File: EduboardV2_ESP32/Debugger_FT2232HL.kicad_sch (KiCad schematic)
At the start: 52 parts, among them Q1 S8050_C139514, Q2 S8050_C139514, U2 FT2232HL, U3 M93C46-WMN6TP, Y2 12MHz

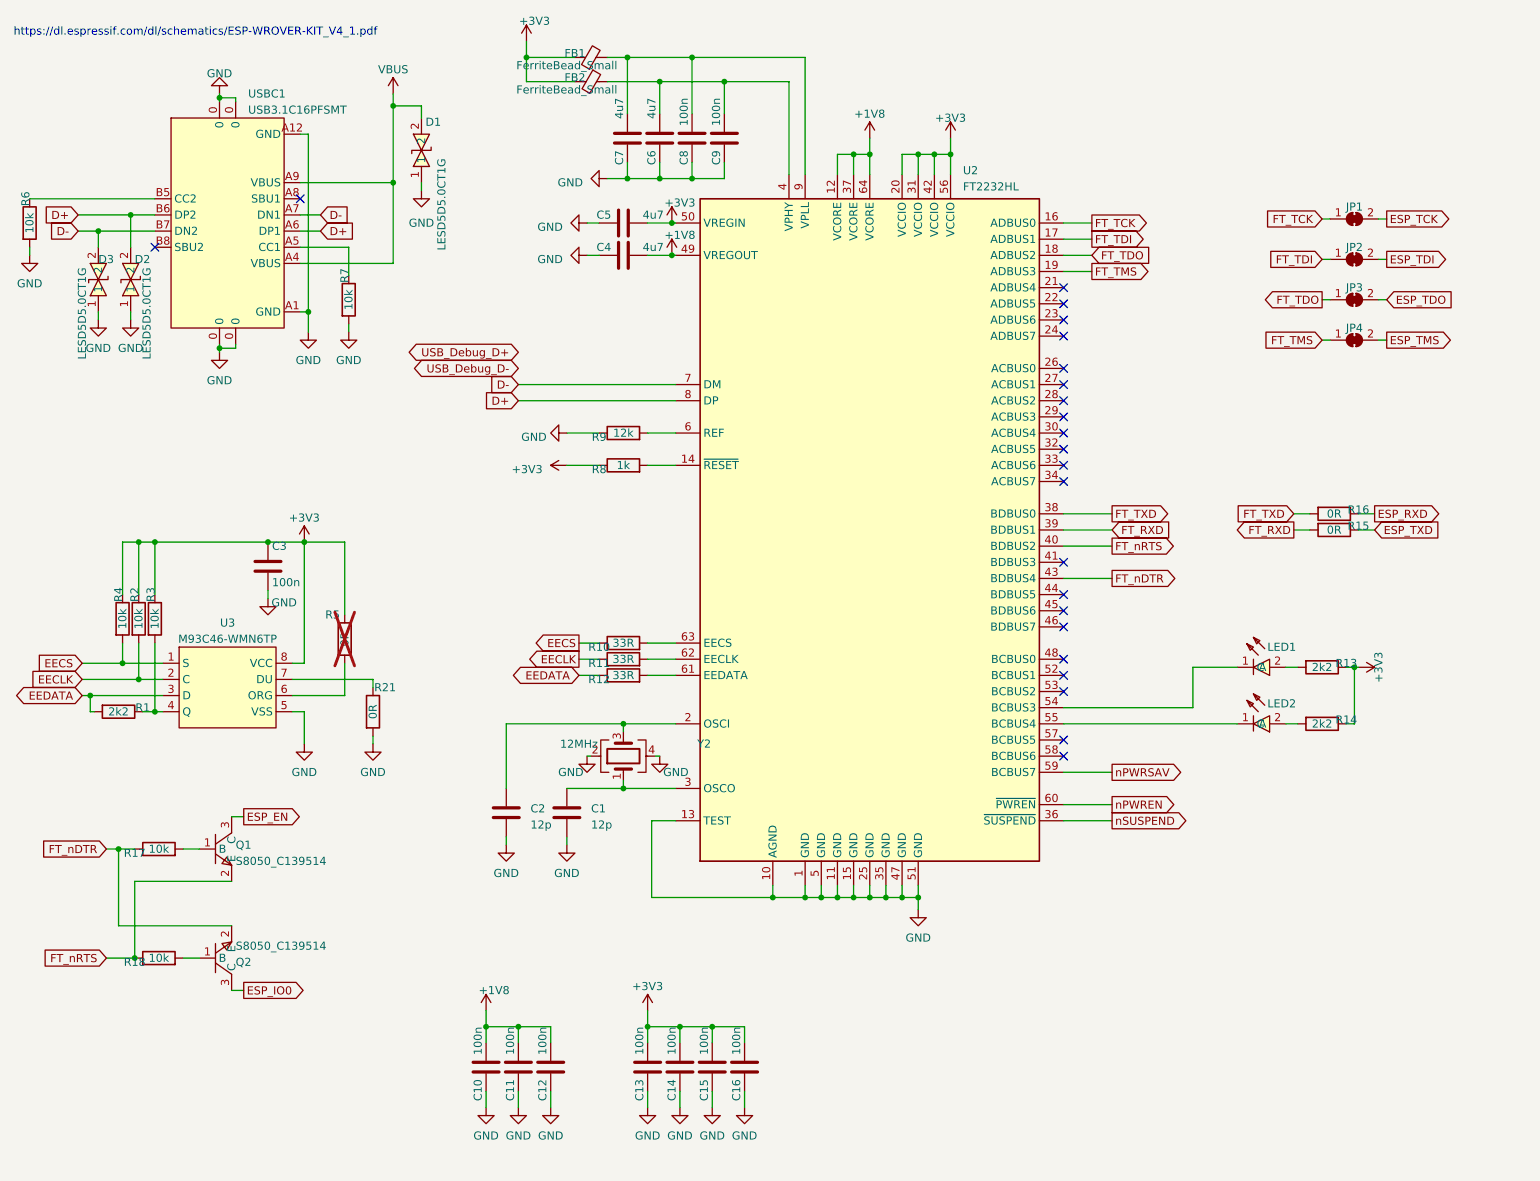
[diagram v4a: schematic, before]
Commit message: add voltage selector to prevent fighting sources
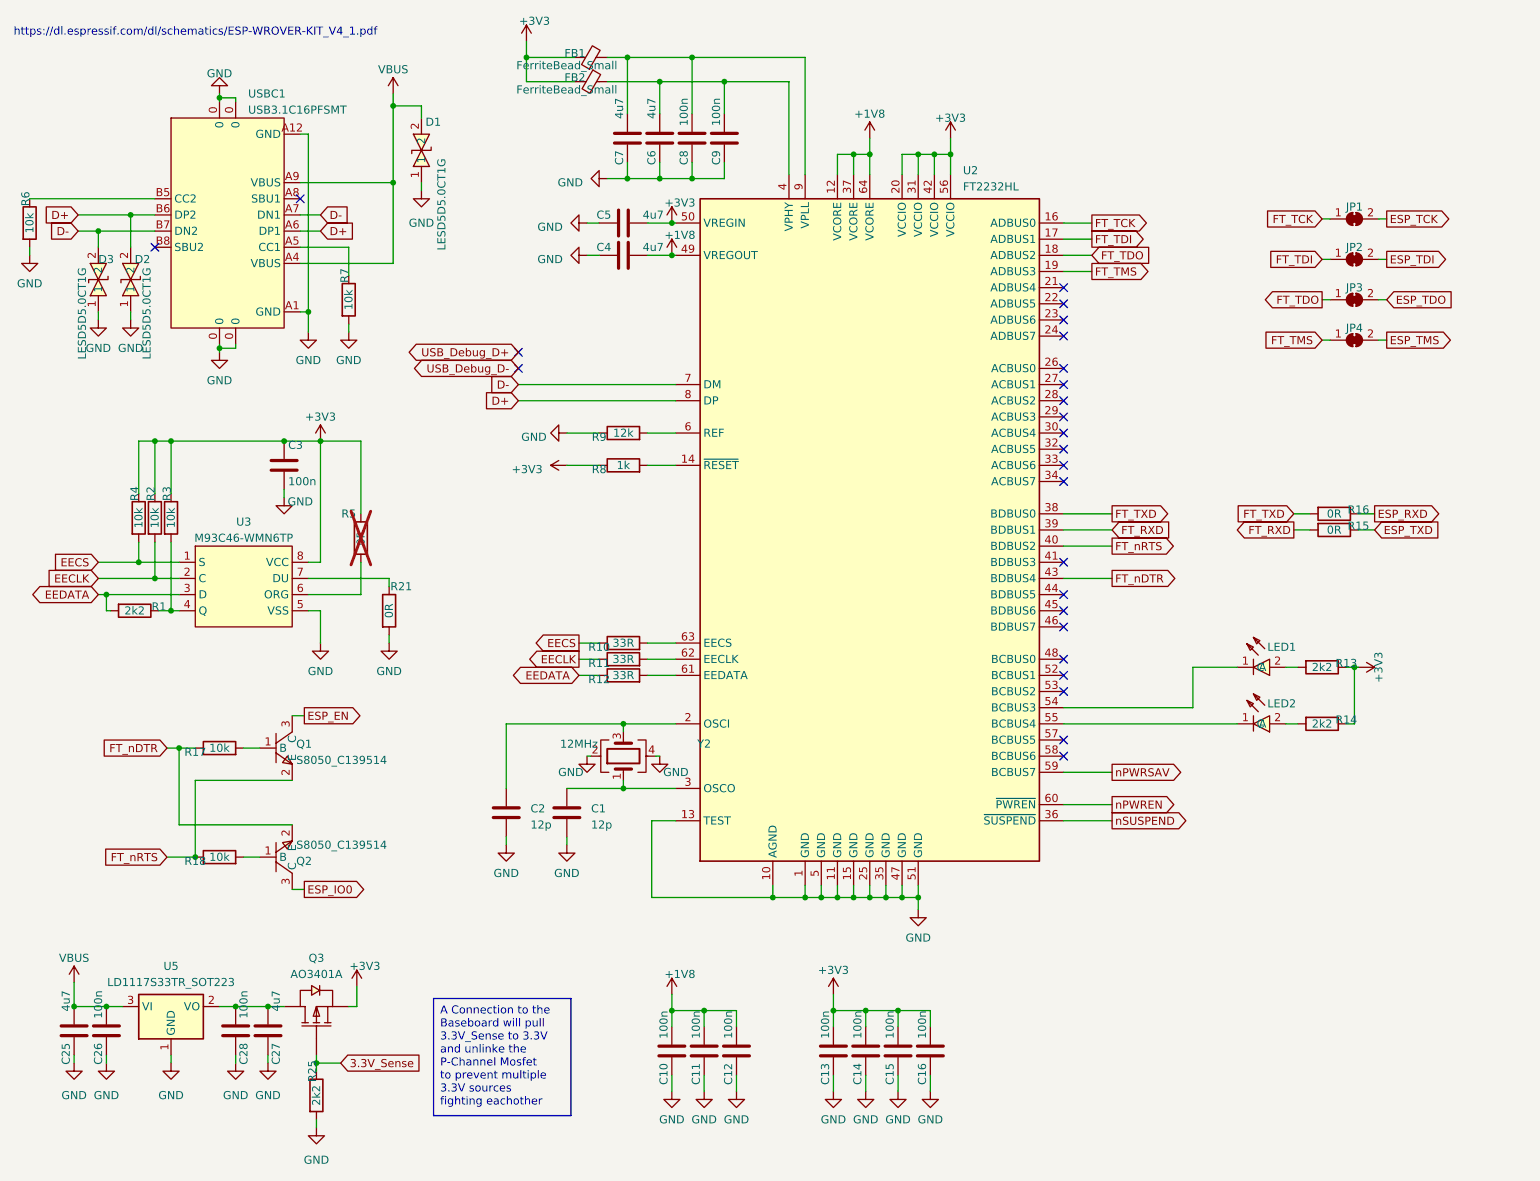
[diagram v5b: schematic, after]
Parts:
- added C25, C27: 4u7, Capacitor_SMD:C_0805_2012Metric, symbol Device:C
- added C26, C28: 100n, Capacitor_SMD:C_0603_1608Metric, symbol Device:C
- added Q3: AO3401A, Package_TO_SOT_SMD:SOT-23-3, symbol eduboardv2:AO3401A
- added R25: 2k2, Resistor_SMD:R_0603_1608Metric, symbol Device:R
- added U5: LD1117S33TR_SOT223, Package_TO_SOT_SMD:SOT-223-3_TabPin2, symbol Regulator_Linear:LD1117S33TR_SOT223
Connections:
- net +3V3: now also Q3.2 (S)
- net GND: now also C25.1, C26.1, C27.1, C28.1, R25.2, U5.1 (GND)
- net VBUS: now also C25.2, C26.2, U5.3 (VI)
- new net: C27.2, C28.2, Q3.3 (D), U5.2 (VO)
- new net 3.3V_Sense: Q3.1 (G), R25.1
- no-connect marks 23 -> 25
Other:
- moved on the sheet: C10, C11, C12, C13, C14, C15, C16, C3, Q1, Q2, R1, R17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

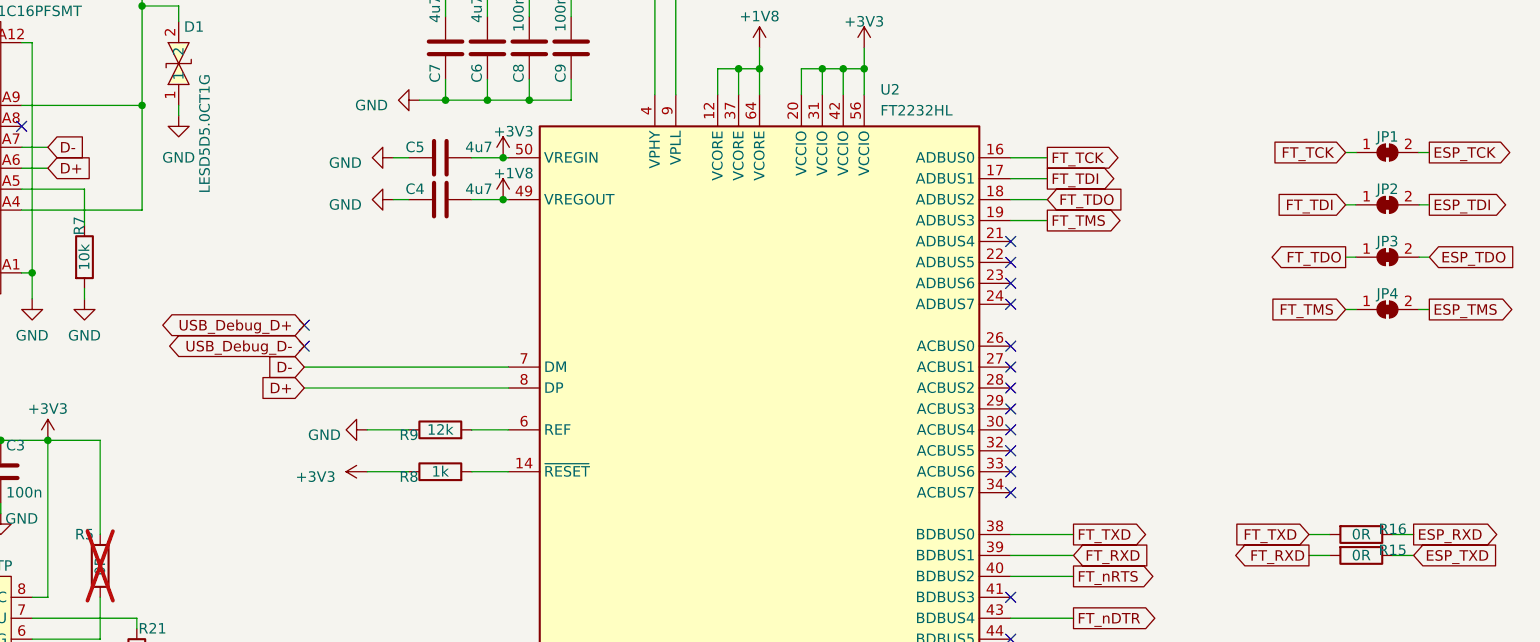
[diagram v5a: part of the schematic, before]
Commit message: resize mPCIE Board Footprint, work on ESP32 UP Board
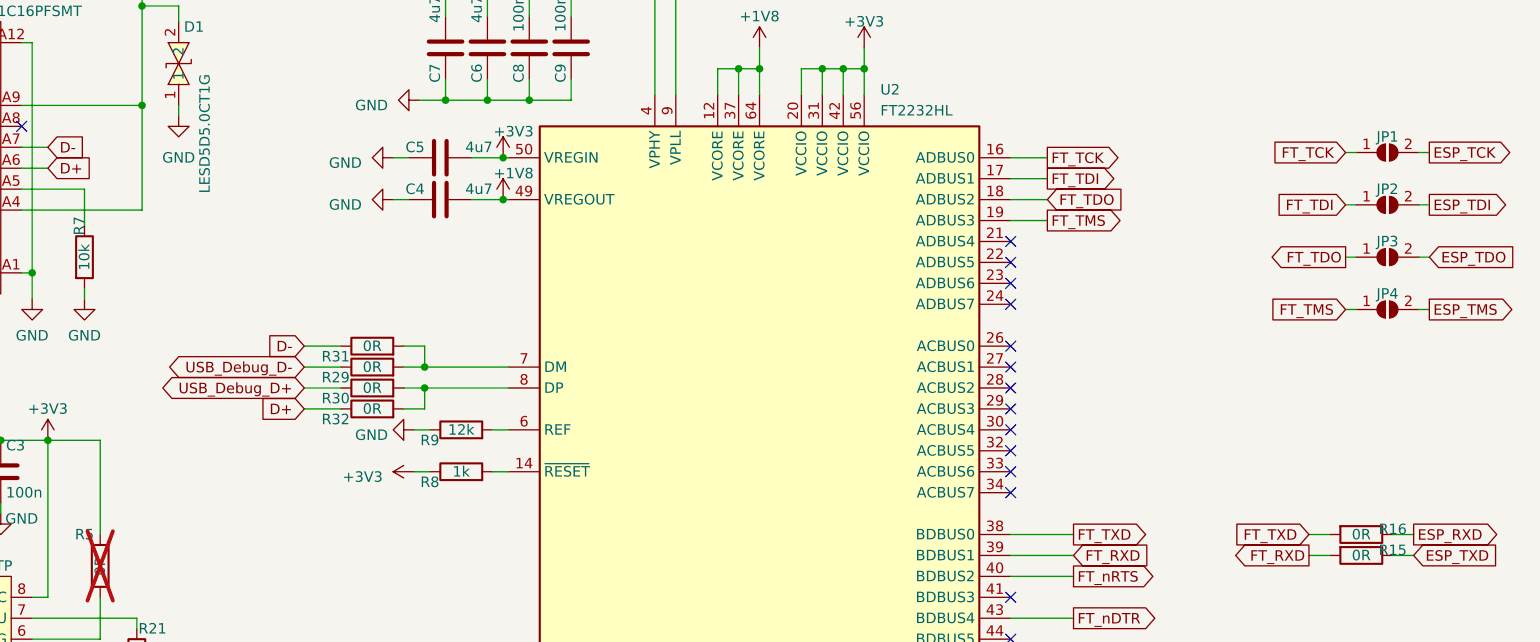
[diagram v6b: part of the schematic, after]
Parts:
- removed JP1, JP2, JP3, JP4: SolderJumper_2_Bridged, Jumper:SolderJumper-2_P1.3mm_Bridged_RoundedPad1.0x1.5mm, symbol Jumper:SolderJumper_2_Bridged
- added JP1, JP2, JP3, JP4: SolderJumper_2_Open, Jumper:SolderJumper-2_P1.3mm_Open_RoundedPad1.0x1.5mm, symbol Jumper:SolderJumper_2_Open
- added R29, R30, R31, R32: 0R, Resistor_SMD:R_0603_1608Metric, symbol Device:R
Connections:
- net D+: now also R32.1; no longer U2.8 (DP)
- net D-: now also R31.1; no longer U2.7 (DM)
- net ESP_TCK: now also JP1.2 (B)
- net ESP_TDI: now also JP2.2 (B)
- net ESP_TDO: now also JP3.2 (B)
- net ESP_TMS: now also JP4.2 (B)
- net FT_TCK: now also JP1.1 (A)
- net FT_TDI: now also JP2.1 (A)
- net FT_TDO: now also JP3.1 (A)
- net FT_TMS: now also JP4.1 (A)
- net USB_Debug_D+: now also R30.1
- net USB_Debug_D-: now also R29.1
- new net: R29.2, R31.2, U2.7 (DM)
- new net: R30.2, R32.2, U2.8 (DP)
- no-connect marks 25 -> 23
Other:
- moved on the sheet: R8, R9

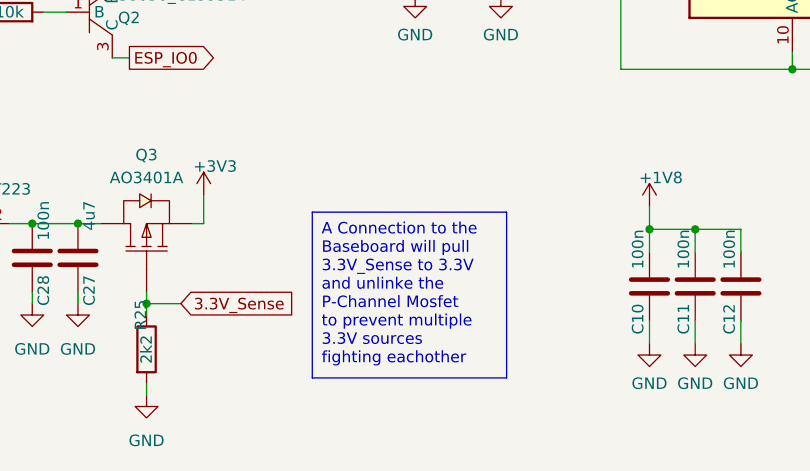
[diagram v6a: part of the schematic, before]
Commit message: layout done so far. Have to check everything and work on footprints in general. Changed to 4 layer (was not possible otherwise)
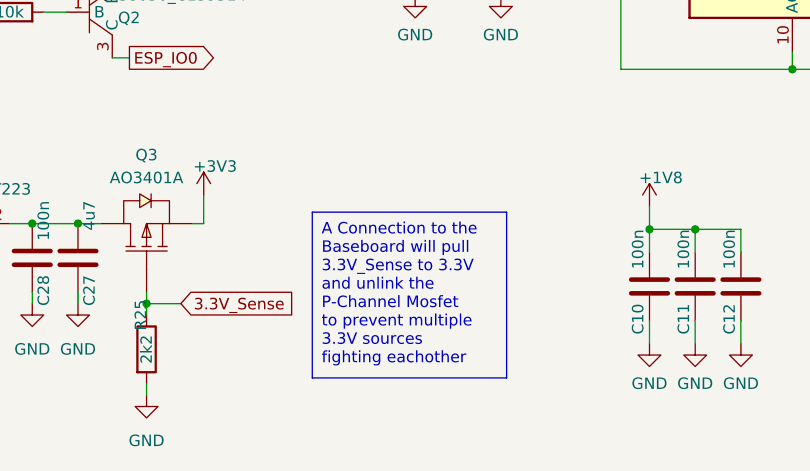
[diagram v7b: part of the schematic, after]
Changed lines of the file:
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@@
     (stroke (width 0) (type default))
   )
-  (text_box "A Connection to the Baseboard will pull 3.3V_Sense to 3.3V and unlinke the P-Channel Mosfet to prevent multiple 3.3V sources fighting eachother"
+  (text_box "A Connection to the Baseboard will pull 3.3V_Sense to 3.3V and unlink the P-Channel Mosfet to prevent multiple 3.3V sources fighting eachother"
     (at 80.645 167.005 0) (size 21.59 18.415)
     (stroke (width 0) (type default))

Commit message: finalize Layout, fill in most of the critical part info. Replace certain parts with Eduboard kicadlib Parts.
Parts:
- FB1, FB2: LCSC Part (none) -> C44838
- Q3: JLCPCB Part # (none) -> C15127
- U5: JLCPCB Part # (none) -> C86781; LCSC Part (none) -> C86781
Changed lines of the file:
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@@
+      (effects (font (size 1.27 1.27)) hide)
+    )
+    (property "LCSC Part" "C44838" (at 105.41 22.86 0)
       (effects (font (size 1.27 1.27)) hide)
     )
@@
       (effects (font (size 1.27 1.27)) hide)
     )
+    (property "JLCPCB Part #" "C15127" (at 62.23 170.815 0)
+      (effects (font (size 1.27 1.27)) hide)
+    )
     (pin "1")
     (pin "2")
@@
       (effects (font (size 1.27 1.27)) hide)
     )
+    (property "LCSC Part" "C44838" (at 105.41 19.05 0)
+      (effects (font (size 1.27 1.27)) hide)
+    )
     (pin "1")
     (pin "2")
@@
       (effects (font (size 1.27 1.27)) hide)
     )
+    (property "JLCPCB Part #" "C86781" (at 39.37 168.275 0)
+      (effects (font (size 1.27 1.27)) hide)
+    )
+    (property "LCSC Part" "C86781" (at 39.37 168.275 0)
+      (effects (font (size 1.27 1.27)) hide)
+    )
